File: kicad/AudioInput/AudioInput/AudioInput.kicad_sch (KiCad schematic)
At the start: 59 parts

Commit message: board routed
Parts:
- removed C15, C16: 1uF, symbol Device:C_Small
- removed J3: (no value), symbol Connector_Generic:Conn_01x04
- removed R28, R30: 100k, symbol Device:R_Small
- removed R29, R31: 150k, symbol Device:R_Small
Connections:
- net AUDIO_INT_IN_L: no longer names the net of U3.1 (Y0)
- net AUDIO_INT_IN_R: no longer names the net of U3.12 (X0)
- no-connect marks 4 -> 6
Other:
- note added: "Audio source selection 3 options: - Line in - Mic in"
- note removed: "Audio source selection 3 options: - Line in - Mic in - Internal header"
- note removed: "Internal audio input header"

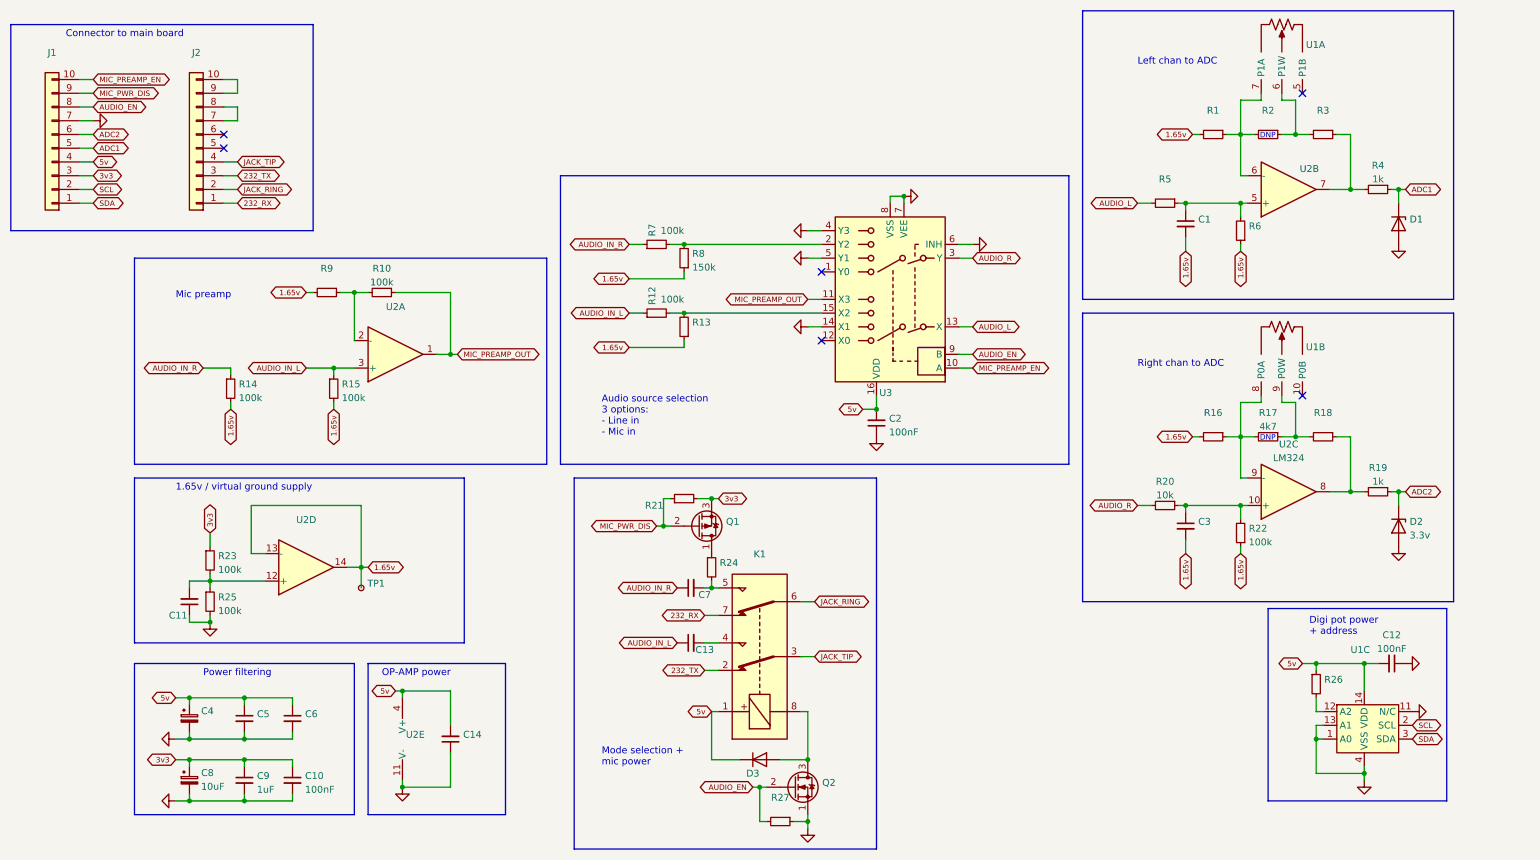
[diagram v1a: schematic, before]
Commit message: audio input with basic threshold pattern working
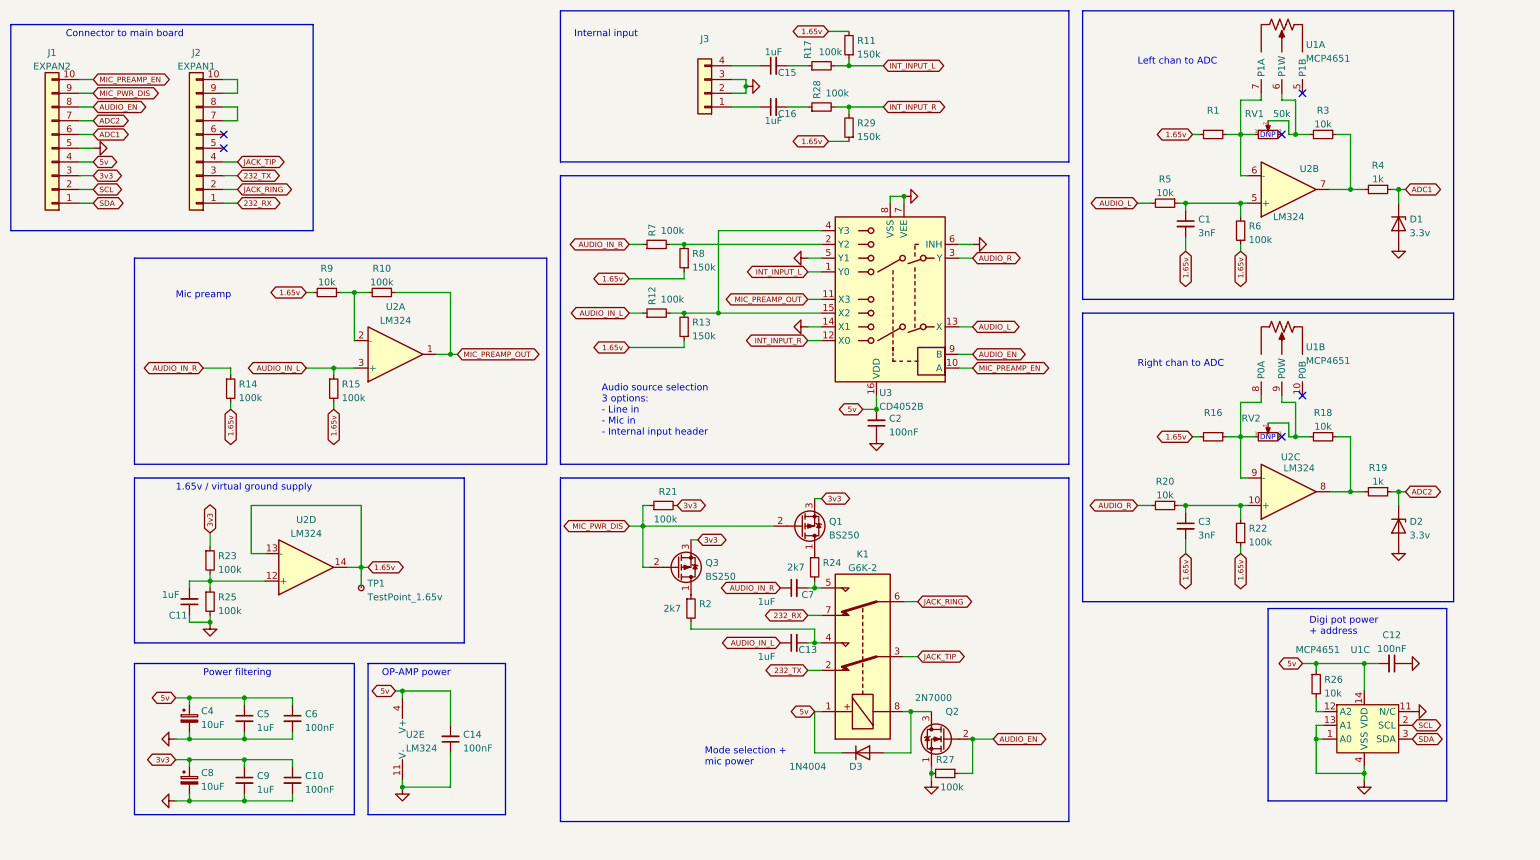
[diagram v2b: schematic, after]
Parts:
- added C15, C16: 1uF, Capacitor_THT:C_Rect_L4.0mm_W2.5mm_P2.50mm, symbol Device:C_Small
- added J3: (no value), symbol Connector_Generic:Conn_01x04
- added Q3: BS250, Package_TO_SOT_THT:TO-92_Inline, symbol Transistor_FET:BS250
- added R11, R29: 150k, Resistor_THT:R_Axial_DIN0207_L6.3mm_D2.5mm_P2.54mm_Vertical, symbol Device:R_Small
- added R28: 100k, Resistor_THT:R_Axial_DIN0207_L6.3mm_D2.5mm_P2.54mm_Vertical, symbol Device:R_Small
- added RV1: 50k, symbol Device:R_Potentiometer_Small
- added RV2: (no value), symbol Device:R_Potentiometer_Small
- C1, C3: value (none) -> 3nF; footprint (none) -> Capacitor_THT:C_Disc_D5.1mm_W3.2mm_P5.00mm
- C10, C12, C2: footprint (none) -> Capacitor_THT:C_Disc_D3.4mm_W2.1mm_P2.50mm
- C11, C13, C5, C7: value (none) -> 1uF; footprint (none) -> Capacitor_THT:C_Rect_L4.0mm_W2.5mm_P2.50mm
- C14, C6: value (none) -> 100nF; footprint (none) -> Capacitor_THT:C_Disc_D3.4mm_W2.1mm_P2.50mm
- C4: value (none) -> 10uF; footprint (none) -> Capacitor_THT:CP_Radial_D5.0mm_P2.00mm
- C8: footprint (none) -> Capacitor_THT:CP_Radial_D5.0mm_P2.00mm
- C9: footprint (none) -> Capacitor_THT:C_Rect_L4.0mm_W2.5mm_P2.50mm
- D1: value (none) -> 3.3v; footprint (none) -> Diode_THT:D_DO-35_SOD27_P2.54mm_Vertical_AnodeUp
- D2: footprint (none) -> Diode_THT:D_DO-35_SOD27_P2.54mm_Vertical_AnodeUp
- D3: value (none) -> 1N4004; footprint (none) -> Diode_THT:D_DO-41_SOD81_P3.81mm_Vertical_AnodeUp
- J1: value (none) -> EXPAN2; footprint (none) -> Connector_PinHeader_2.54mm:PinHeader_1x10_P2.54mm_Vertical
- J2: value (none) -> EXPAN1; footprint (none) -> Connector_PinHeader_2.54mm:PinHeader_1x10_P2.54mm_Vertical
- K1: value (none) -> G6K-2; footprint (none) -> Relay_SMD:Relay_DPDT_Omron_G6K-2F-Y
- Q1: value (none) -> BS250; footprint (none) -> Package_TO_SOT_THT:TO-92_Inline
- Q2: value (none) -> 2N7000; footprint (none) -> Package_TO_SOT_THT:TO-92_Inline
- R10, R12, R14, R15, R19, R20, R22, R23, R25, R4, R7, R8: footprint (none) -> Resistor_THT:R_Axial_DIN0207_L6.3mm_D2.5mm_P2.54mm_Vertical
- R13: value (none) -> 150k; footprint (none) -> Resistor_THT:R_Axial_DIN0207_L6.3mm_D2.5mm_P2.54mm_Vertical
- R17: value 4k7 -> 100k; footprint (none) -> Resistor_THT:R_Axial_DIN0207_L6.3mm_D2.5mm_P2.54mm_Vertical
- R18, R26, R3, R5, R9: value (none) -> 10k; footprint (none) -> Resistor_THT:R_Axial_DIN0207_L6.3mm_D2.5mm_P2.54mm_Vertical
- R2, R24: value (none) -> 2k7; footprint (none) -> Resistor_THT:R_Axial_DIN0207_L6.3mm_D2.5mm_P2.54mm_Vertical
- R21, R27, R6: value (none) -> 100k; footprint (none) -> Resistor_THT:R_Axial_DIN0207_L6.3mm_D2.5mm_P2.54mm_Vertical
- TP1: value (none) -> TestPoint_1.65v; footprint (none) -> TestPoint:TestPoint_Pad_D1.5mm
- U1: value (none) -> MCP4651; footprint (none) -> Package_SO:TSSOP-14_4.4x5mm_P0.65mm
- U2: value (none) -> LM324; footprint (none) -> Package_DIP:DIP-14_W7.62mm_Socket
- U3: value (none) -> CD4052B; footprint (none) -> Package_DIP:DIP-16_W7.62mm_Socket
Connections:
- net 1.65v: now also R11.2, R29.1
- net 3v3: now also Q3.3 (S)
- net ADC1: now also J1.6 (Pin_6); no longer J1.5 (Pin_5)
- net ADC2: now also J1.7 (Pin_7); no longer J1.6 (Pin_6)
- net AUDIO_EN: now also R27.1; no longer R27.2
- net GND: now also J1.5 (Pin_5), R27.2, J3.2 (Pin_2), J3.3 (Pin_3); no longer J1.7 (Pin_7), R27.1, U3.4 (Y3)
- net MIC_PWR_DIS: now also Q3.2 (G)
- net at R1.1, U1.7 (P1A), U2.6 (-): now also RV1.1; no longer R2.2
- net INT_INPUT_L: now reaches U3.1 (Y0)
- net INT_INPUT_L: now also R17.2, R11.1
- net INT_INPUT_R: now reaches U3.12 (X0)
- net INT_INPUT_R: now also R28.2, R29.2
- net at R12.2, R13.2, U3.15 (X2): now also U3.4 (Y3)
- net at R18.2, U1.9 (P0W): now also RV2.2; no longer R17.1
- net at R16.1, U1.8 (P0A), U2.9 (-): now also RV2.1; no longer R17.2
- net at R3.2, U1.6 (P1W): now also RV1.2; no longer R2.1
- net at C13.2, K1.4: now also R2.2
- new net: C15.2, R17.1
- new net: C15.1, J3.4 (Pin_4)
- new net: Q3.1 (D), R2.1
- new net: C16.1, J3.1 (Pin_1)
- new net: C16.2, R28.1
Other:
- note added: "Audio source selection 3 options: - Line in - Mic in - Internal input header"
- note added: "Internal input"
- note removed: "Audio source selection 3 options: - Line in - Mic in"
- moved on the sheet: C13, C7, D3, K1, Q1, Q2, R21, R24, R27

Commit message: mostly documentation of audio input board
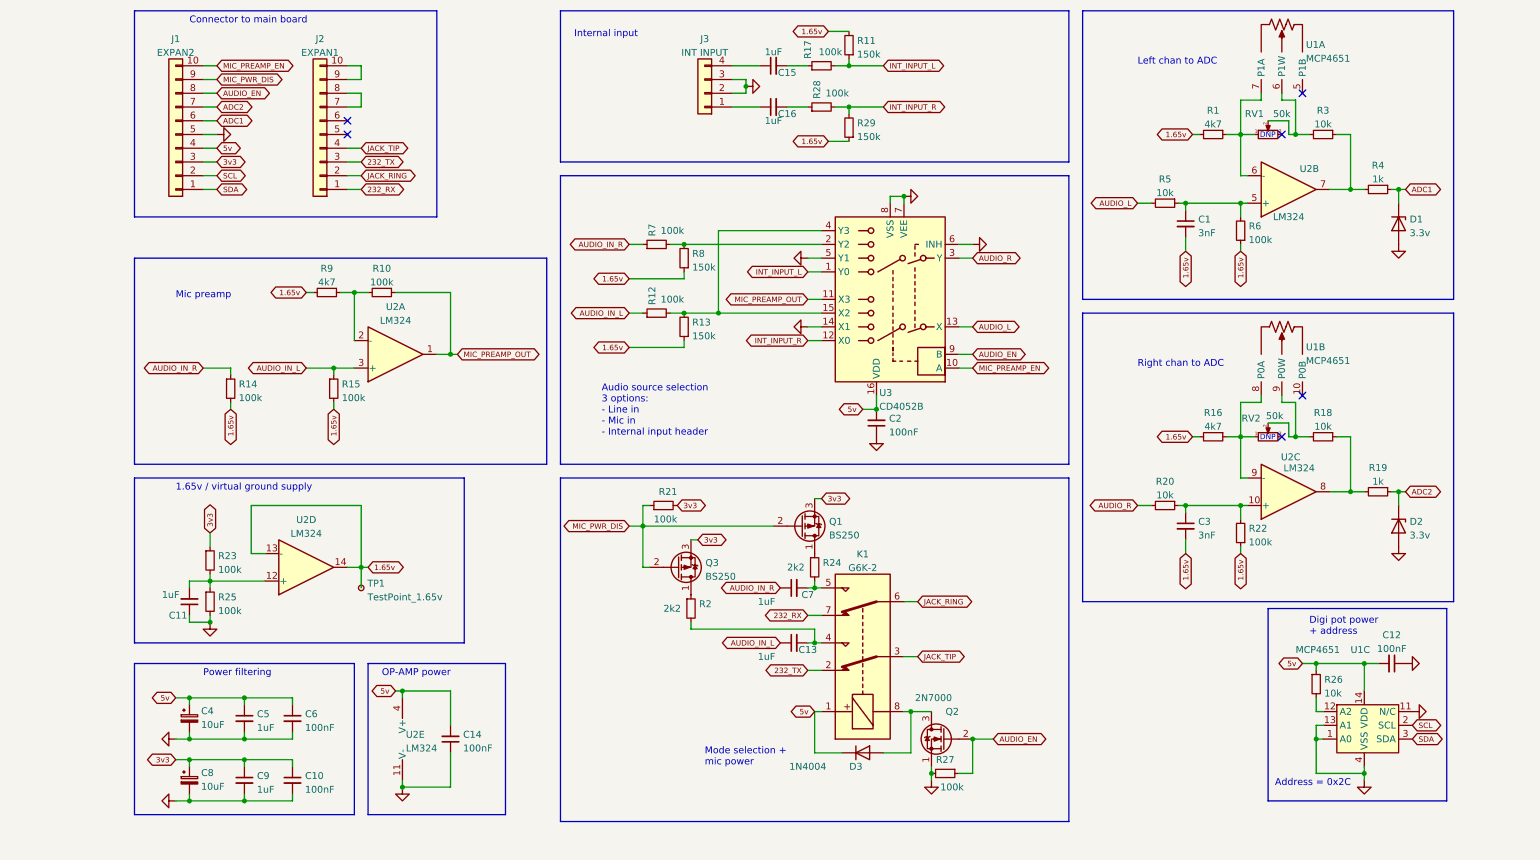
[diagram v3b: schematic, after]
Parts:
- J3: value (none) -> INT INPUT; footprint (none) -> Connector_PinHeader_2.54mm:PinHeader_1x04_P2.54mm_Vertical
- R1, R16: value (none) -> 4k7; footprint (none) -> Resistor_THT:R_Axial_DIN0207_L6.3mm_D2.5mm_P2.54mm_Vertical
- R2, R24: value 2k7 -> 2k2
- R9: value 10k -> 4k7
- RV1: footprint (none) -> Library:3362P-1-503
- RV2: value (none) -> 50k; footprint (none) -> Library:3362P-1-503
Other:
- note added: "Address = 0x2C"
- company: (none) -> CrashOverride85
- title: (none) -> ZC95 Audio Input 
- moved on the sheet: J1, J2

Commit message: Audio input board v0.4
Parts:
- removed C13: 1uF, Capacitor_THT:C_Rect_L4.0mm_W2.5mm_P2.50mm, symbol Device:C_Small
- removed C8: 10uF, Capacitor_THT:CP_Radial_D5.0mm_P2.00mm, symbol Device:C_Polarized_Small
- removed D1, D2: 3.3v, Diode_THT:D_DO-35_SOD27_P2.54mm_Vertical_AnodeUp, symbol Device:D_Zener
- removed Q1, Q3: BS250, Package_TO_SOT_THT:TO-92_Inline, symbol Transistor_FET:BS250
- removed Q2: 2N7000, Package_TO_SOT_THT:TO-92_Inline, symbol Transistor_FET:2N7000
- removed RV1, RV2: 50k, Library:3362P-1-503, symbol Device:R_Potentiometer_Small
- added C13: 10uF, Capacitor_SMD:C_0603_1608Metric_Pad1.08x0.95mm_HandSolder, symbol Device:C_Polarized_Small
- added C8: 1uF, Capacitor_SMD:C_0603_1608Metric_Pad1.08x0.95mm_HandSolder, symbol Device:C_Small
- added Q1, Q2: AO3401A, Package_TO_SOT_SMD:SOT-23, symbol Transistor_FET:AO3401A
- added Q3: AO3400A, Package_TO_SOT_SMD:SOT-23, symbol Transistor_FET:AO3400A
- C1: value 3nF -> 3.3nF; footprint Capacitor_THT:C_Disc_D5.1mm_W3.2mm_P5.00mm -> Capacitor_SMD:C_0603_1608Metric_Pad1.08x0.95mm_HandSolder; LCSC C454433 -> C1613
- C10, C12, C6: footprint Capacitor_THT:C_Disc_D3.4mm_W2.1mm_P2.50mm -> Capacitor_SMD:C_0603_1608Metric_Pad1.08x0.95mm_HandSolder; LCSC (none) -> C14663
- C11, C15, C7, C9: footprint Capacitor_THT:C_Rect_L4.0mm_W2.5mm_P2.50mm -> Capacitor_SMD:C_0603_1608Metric_Pad1.08x0.95mm_HandSolder; LCSC (none) -> C15849
- C14, C2: value 100nF -> 1uF; footprint Capacitor_THT:C_Disc_D3.4mm_W2.1mm_P2.50mm -> Capacitor_SMD:C_0603_1608Metric_Pad1.08x0.95mm_HandSolder; LCSC (none) -> C15849
- C16: value 1uF -> 100nF; footprint Capacitor_THT:C_Rect_L4.0mm_W2.5mm_P2.50mm -> Capacitor_SMD:C_0603_1608Metric_Pad1.08x0.95mm_HandSolder; LCSC (none) -> C14663
- C3: value 3nF -> 100nF; footprint Capacitor_THT:C_Disc_D5.1mm_W3.2mm_P5.00mm -> Capacitor_SMD:C_0603_1608Metric_Pad1.08x0.95mm_HandSolder; LCSC C454433 -> C14663
- C4: footprint Capacitor_THT:CP_Radial_D5.0mm_P2.00mm -> Capacitor_SMD:C_0603_1608Metric_Pad1.08x0.95mm_HandSolder; LCSC (none) -> C19702
- C5: value 1uF -> 3.3nF; footprint Capacitor_THT:C_Rect_L4.0mm_W2.5mm_P2.50mm -> Capacitor_SMD:C_0603_1608Metric_Pad1.08x0.95mm_HandSolder; LCSC (none) -> C1613
- D3: value 1N4004 -> SM4007PL; footprint Diode_THT:D_DO-41_SOD81_P3.81mm_Vertical_AnodeUp -> Diode_SMD:D_SOD-123F; LCSC (none) -> C64898
- K1: LCSC (none) -> C47190
- R1: footprint Resistor_THT:R_Axial_DIN0207_L6.3mm_D2.5mm_P2.54mm_Vertical -> Resistor_SMD:R_0603_1608Metric_Pad0.98x0.95mm_HandSolder; LCSC (none) -> C23162
- R10: value 100k -> 4k7; footprint Resistor_THT:R_Axial_DIN0207_L6.3mm_D2.5mm_P2.54mm_Vertical -> Resistor_SMD:R_0603_1608Metric_Pad0.98x0.95mm_HandSolder; LCSC (none) -> C23162
- R11, R29: footprint Resistor_THT:R_Axial_DIN0207_L6.3mm_D2.5mm_P2.54mm_Vertical -> Resistor_SMD:R_0603_1608Metric_Pad0.98x0.95mm_HandSolder; LCSC (none) -> C22807
- R12, R15, R17, R21, R23, R25, R27, R28, R7: footprint Resistor_THT:R_Axial_DIN0207_L6.3mm_D2.5mm_P2.54mm_Vertical -> Resistor_SMD:R_0603_1608Metric_Pad0.98x0.95mm_HandSolder; LCSC (none) -> C25803
- R13, R8: value 150k -> 100k; footprint Resistor_THT:R_Axial_DIN0207_L6.3mm_D2.5mm_P2.54mm_Vertical -> Resistor_SMD:R_0603_1608Metric_Pad0.98x0.95mm_HandSolder; LCSC (none) -> C25803
- R14: value 100k -> 150k; footprint Resistor_THT:R_Axial_DIN0207_L6.3mm_D2.5mm_P2.54mm_Vertical -> Resistor_SMD:R_0603_1608Metric_Pad0.98x0.95mm_HandSolder; LCSC (none) -> C22807
- R16: value 4k7 -> 100k; footprint Resistor_THT:R_Axial_DIN0207_L6.3mm_D2.5mm_P2.54mm_Vertical -> Resistor_SMD:R_0603_1608Metric_Pad0.98x0.95mm_HandSolder; LCSC (none) -> C25803
- R18: value 10k -> 4k7; footprint Resistor_THT:R_Axial_DIN0207_L6.3mm_D2.5mm_P2.54mm_Vertical -> Resistor_SMD:R_0603_1608Metric_Pad0.98x0.95mm_HandSolder; LCSC (none) -> C23162
- R19: value 1k -> 10k; footprint Resistor_THT:R_Axial_DIN0207_L6.3mm_D2.5mm_P2.54mm_Vertical -> Resistor_SMD:R_0603_1608Metric_Pad0.98x0.95mm_HandSolder; LCSC (none) -> C25804
- R2, R24: footprint Resistor_THT:R_Axial_DIN0207_L6.3mm_D2.5mm_P2.54mm_Vertical -> Resistor_SMD:R_0603_1608Metric_Pad0.98x0.95mm_HandSolder; LCSC (none) -> C4190
- R20: value 10k -> 1k; footprint Resistor_THT:R_Axial_DIN0207_L6.3mm_D2.5mm_P2.54mm_Vertical -> Resistor_SMD:R_0603_1608Metric_Pad0.98x0.95mm_HandSolder; LCSC (none) -> C21190
- R22, R6: value 100k -> 10k; footprint Resistor_THT:R_Axial_DIN0207_L6.3mm_D2.5mm_P2.54mm_Vertical -> Resistor_SMD:R_0603_1608Metric_Pad0.98x0.95mm_HandSolder; LCSC (none) -> C25804
- R26, R3: footprint Resistor_THT:R_Axial_DIN0207_L6.3mm_D2.5mm_P2.54mm_Vertical -> Resistor_SMD:R_0603_1608Metric_Pad0.98x0.95mm_HandSolder; LCSC (none) -> C25804
- R4: footprint Resistor_THT:R_Axial_DIN0207_L6.3mm_D2.5mm_P2.54mm_Vertical -> Resistor_SMD:R_0603_1608Metric_Pad0.98x0.95mm_HandSolder; LCSC (none) -> C21190
- R5: value 10k -> 100k; footprint Resistor_THT:R_Axial_DIN0207_L6.3mm_D2.5mm_P2.54mm_Vertical -> Resistor_SMD:R_0603_1608Metric_Pad0.98x0.95mm_HandSolder; LCSC (none) -> C25803
- R9: value 4k7 -> 150k; footprint Resistor_THT:R_Axial_DIN0207_L6.3mm_D2.5mm_P2.54mm_Vertical -> Resistor_SMD:R_0603_1608Metric_Pad0.98x0.95mm_HandSolder; LCSC (none) -> C22807
- U1: LCSC (none) -> C148010
- U2: footprint Package_DIP:DIP-14_W7.62mm_Socket -> Package_SO:SOIC-14_3.9x8.7mm_P1.27mm; LCSC (none) -> C71035
- U3: footprint Package_DIP:DIP-16_W7.62mm_Socket -> Package_SO:SOIC-16_3.9x9.9mm_P1.27mm; LCSC (none) -> C6521
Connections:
- net 1.65v: now also C5.2, R10.2, R14.1, R15.1, R16.1, R18.2, R23.1, R9.1; no longer C3.2, R13.1, R14.2, R15.2, R16.2, R22.1, R6.1, R9.2
- net 3v3: now also C14.2, C16.1, R25.2, C13.1, Q1.2 (S), Q2.2 (S); no longer C10.1, C9.1, R23.1
- net 5v: now also C10.1, C11.2, C12.1, C3.2, R28.1; no longer C12.2, C14.2, C2.2, C5.1
- net ADC2: now also R20.1; no longer R19.1
- net AUDIO_EN: now also R28.2, Q3.1 (G); no longer R27.1
- net AUDIO_IN_L: now also C9.1, R13.1, R16.2; no longer R12.1, R15.1
- net AUDIO_IN_R: now also R15.2; no longer R14.1
- net AUDIO_L: now also R6.2; no longer R5.2
- net AUDIO_R: now also R22.2; no longer R20.2
- net GND: now also C12.2, C16.2, C3.1, C13.2, C8.1, Q3.2 (S); no longer C12.1, C2.1, C5.2, C9.2, R25.2
- net INT_INPUT_R: now also R5.2; no longer R28.2
- net MIC_PREAMP_OUT: now also R12.2; no longer R10.1
- net MIC_PWR_DIS: now also Q1.1 (G), Q2.1 (G)
- net at R7.2, U3.2 (Y2): now also R9.2; no longer R8.2
- net at R13.2, U3.15 (X2), U3.4 (Y3): now also R14.2; no longer R12.2
- net at U1.9 (P0W): now also R19.2; no longer R18.2
- net at R25.1, U2.12 (+): now also R27.1, C8.2; no longer C11.2, R23.2
- net at U1.8 (P0A), U2.9 (-): now also R18.1; no longer R16.1
- net at C1.1, U2.5 (+): now also R6.1, R8.2; no longer R5.1, R6.2
- net at R2.1: now also Q2.3 (D)
- net at K1.4, R2.2: now also C9.2
- net at J3.1 (Pin_1): now also C2.1; no longer C16.1
- net at R24.1: now also Q1.3 (D)
- net at D3.2 (A), K1.8: now also Q3.3 (D)
- new net: C5.1, R22.1, R23.2, U2.10 (+)
- new net: R19.1, R20.2, U2.8
- new net: R10.1, R12.1, U2.2 (-)
- new net: C2.2, R5.1
- no-connect marks 6 -> 4
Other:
- note removed: "DNP"
